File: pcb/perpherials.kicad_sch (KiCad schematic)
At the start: 9 parts, among them J4 TC2030, J6 050700622, J6 SBH11-PBPC-D05-ST-BK, U6 M24C64-FCS6TP/K, U7 BNO055

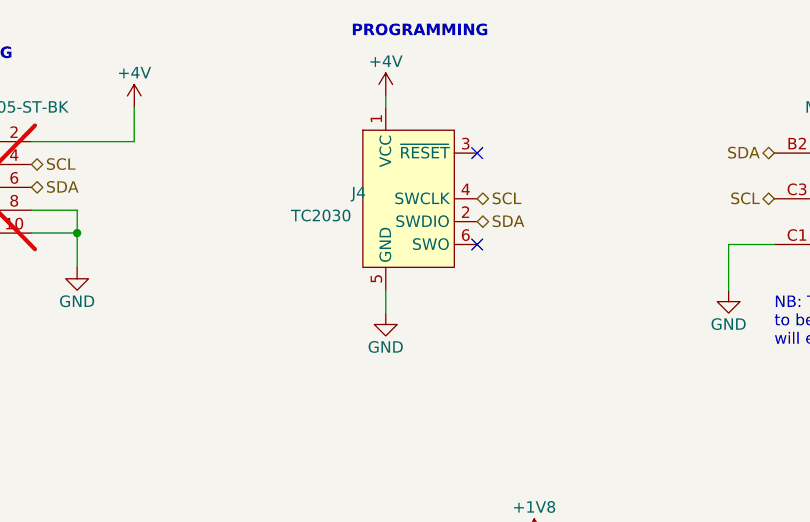
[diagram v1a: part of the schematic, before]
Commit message: Revision B
- Fix incorrect STG3856 symbol and make corresponding changes to PCB
- Flip bits 1 and 2 in probe interaces (fixes #1)
- Improve silkscreen
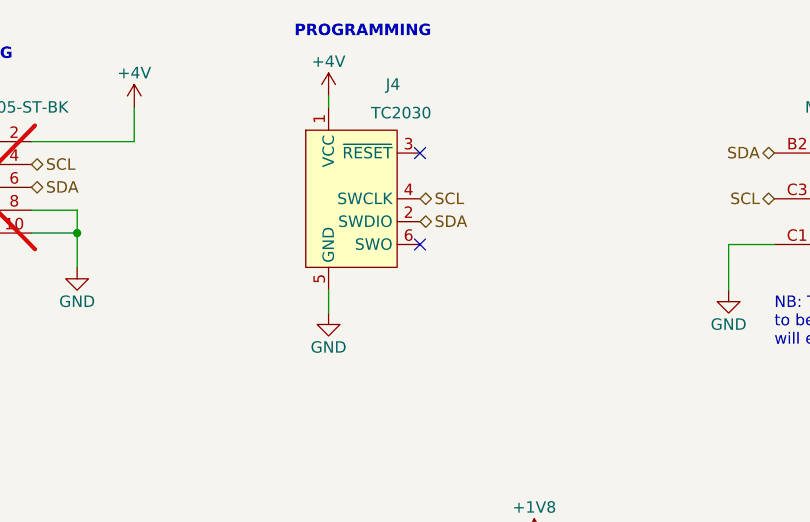
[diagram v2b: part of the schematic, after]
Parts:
- C25, C26, C27, C28, J4, J6, U6, U7: OEPS PN (none) -> ??
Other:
- moved on the sheet: J4
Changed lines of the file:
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@@
   (title_block
     (title "ONIX Neuropixels 2.0 Economical Headstage")
-    (rev "A")
+    (rev "B")
     (company "Open Ephys, Inc")
     (comment 1 "Jonathan P. Newman")
@@
   )
   (no_connect (at 114.3 127))
-  (no_connect (at 153.67 64.77))
+  (no_connect (at 147.32 64.77))
   (no_connect (at 144.78 127))
   (no_connect (at 114.3 119.38))
   (no_connect (at 144.78 114.3))
-  (no_connect (at 153.67 54.61))
+  (no_connect (at 147.32 54.61))
   (wire (pts (xy 115.57 53.34) (xy 115.57 49.53))
     (stroke (width 0) (type default))
@@
     (stroke (width 0) (type default))
   )
-  (wire (pts (xy 143.51 48.26) (xy 143.51 49.53))
-    (stroke (width 0) (type default))
-  )
-  (wire (pts (xy 143.51 69.85) (xy 143.51 72.39))
+  (wire (pts (xy 137.16 48.26) (xy 137.16 49.53))
+    (stroke (width 0) (type default))
+  )
+  (wire (pts (xy 137.16 69.85) (xy 137.16 72.39))
     (stroke (width 0) (type default))
   )
@@
     (effects (font (size 1.27 1.27) (thickness 0.254) bold) (justify left bottom))
   )
-  (text "PROGRAMMING" (at 139.7 41.91 0)
+  (text "PROGRAMMING" (at 133.35 41.91 0)
     (effects (font (size 1.27 1.27) (thickness 0.254) bold) (justify left bottom))
   )
@@
     (effects (font (size 1.27 1.27)) (justify right))
   )
-  (hierarchical_label "SDA" (shape bidirectional) (at 153.67 62.23 0) (fields_autoplaced)
+  (hierarchical_label "SDA" (shape bidirectional) (at 147.32 62.23 0) (fields_autoplaced)
     (effects (font (size 1.27 1.27)) (justify left))
   )
@@
     (effects (font (size 1.27 1.27)) (justify left))
   )
-  (hierarchical_label "SCL" (shape bidirectional) (at 153.67 59.69 0) (fields_autoplaced)
+  (hierarchical_label "SCL" (shape bidirectional) (at 147.32 59.69 0) (fields_autoplaced)
     (effects (font (size 1.27 1.27)) (justify left))
   )
-  (symbol (lib_id "power:GND") (at 143.51 72.39 0) (mirror y) (unit 1)
-    (in_bom yes) (on_board yes) (dnp no)
-    (property "Reference" "#PWR060" (at 143.51 78.74 0)
-      (effects (font (size 1.27 1.27)) hide)
-    )
-    (property "Value" "GND" (at 143.51 76.2 0)
-      (effects (font (size 1.27 1.27)))
-    )
-    (property "Footprint" "" (at 143.51 72.39 0)
-      (effects (font (size 1.27 1.27)) hide)
-    )
-    (property "Datasheet" "" (at 143.51 72.39 0)
+  (symbol (lib_id "power:GND") (at 137.16 72.39 0) (mirror y) (unit 1)
+    (in_bom yes) (on_board yes) (dnp no)
+    (property "Reference" "#PWR060" (at 137.16 78.74 0)
+      (effects (font (size 1.27 1.27)) hide)
+    )
+    (property "Value" "GND" (at 137.16 76.2 0)
+      (effects (font (size 1.27 1.27)))
+    )
+    (property "Footprint" "" (at 137.16 72.39 0)
+      (effects (font (size 1.27 1.27)) hide)
+    )
+    (property "Datasheet" "" (at 137.16 72.39 0)
       (effects (font (size 1.27 1.27)) hide)
     )
@@
     )
     (property "Tolerance" "" (at 129.54 127 0)
+      (effects (font (size 1.27 1.27)) hide)
+    )
+    (property "OEPS PN" "??" (at 129.54 127 0)
       (effects (font (size 1.27 1.27)) hide)
     )
@@
       (effects (font (size 1.27 1.27)) hide)
     )
+    (property "OEPS PN" "??" (at 214.63 125.73 0)
+      (effects (font (size 1.27 1.27)) hide)
+    )
     (pin "1")
     (pin "2")
@@
       (effects (font (size 1.27 1.27)) hide)
     )
+    (property "OEPS PN" "??" (at 217.17 59.69 0)
+      (effects (font (size 1.27 1.27)) hide)
+    )
     (pin "1")
     (pin "2")
@@
     )
     (property "Tolerance" "" (at 198.12 59.69 0)
+      (effects (font (size 1.27 1.27)) hide)
+    )
+    (property "OEPS PN" "??" (at 198.12 59.69 0)
       (effects (font (size 1.27 1.27)) hide)
     )
@@
       (effects (font (size 1.27 1.27)) hide)
     )
+    (property "OEPS PN" "??" (at 87.63 110.49 0)
+      (effects (font (size 1.27 1.27)) hide)
+    )
     (pin "1")
     (pin "2")
@@
     )
   )
-  (symbol (lib_id "Connector:Conn_ARM_SWD_TagConnect_TC2030") (at 146.05 59.69 0) (unit 1)
+  (symbol (lib_id "Connector:Conn_ARM_SWD_TagConnect_TC2030") (at 139.7 59.69 0) (unit 1)
     (in_bom no) (on_board yes) (dnp no)
-    (property "Reference" "J4" (at 139.7 59.055 0)
+    (property "Reference" "J4" (at 143.51 46.99 0)
       (effects (font (size 1.27 1.27)) (justify left))
     )
-    (property "Value" "TC2030" (at 139.7 61.595 0)
+    (property "Value" "TC2030" (at 148.59 50.165 0)
       (effects (font (size 1.27 1.27)) (justify right))
     )
-    (property "Footprint" "Connector:Tag-Connect_TC2030-IDC-FP_2x03_P1.27mm_Vertical" (at 146.05 77.47 0)
-      (effects (font (size 1.27 1.27)) hide)
-    )
-    (property "Datasheet" "https://www.tag-connect.com/wp-content/uploads/bsk-pdf-manager/TC2030-CTX_1.pdf" (at 146.05 74.93 0)
-      (effects (font (size 1.27 1.27)) hide)
-    )
-    (property "Tolerance" "" (at 146.05 59.69 0)
+    (property "Footprint" "Connector:Tag-Connect_TC2030-IDC-FP_2x03_P1.27mm_Vertical" (at 139.7 77.47 0)
+      (effects (font (size 1.27 1.27)) hide)
+    )
+    (property "Datasheet" "https://www.tag-connect.com/wp-content/uploads/bsk-pdf-manager/TC2030-CTX_1.pdf" (at 139.7 74.93 0)
+      (effects (font (size 1.27 1.27)) hide)
+    )
+    (property "Tolerance" "" (at 139.7 59.69 0)
+      (effects (font (size 1.27 1.27)) hide)
+    )
+    (property "OEPS PN" "??" (at 139.7 59.69 0)
       (effects (font (size 1.27 1.27)) hide)
     )
@@
     )
   )
-  (symbol (lib_id "power:+4V") (at 143.51 48.26 0) (mirror y) (unit 1)
+  (symbol (lib_id "power:+4V") (at 137.16 48.26 0) (mirror y) (unit 1)
     (in_bom yes) (on_board yes) (dnp no) (fields_autoplaced)
-    (property "Reference" "#PWR06" (at 143.51 52.07 0)
-      (effects (font (size 1.27 1.27)) hide)
-    )
-    (property "Value" "+4V" (at 143.51 44.45 0)
-      (effects (font (size 1.27 1.27)))
-    )
-    (property "Footprint" "" (at 143.51 48.26 0)
-      (effects (font (size 1.27 1.27)) hide)
-    )
-    (property "Datasheet" "" (at 143.51 48.26 0)
+    (property "Reference" "#PWR06" (at 137.16 52.07 0)
+      (effects (font (size 1.27 1.27)) hide)
+    )
+    (property "Value" "+4V" (at 137.16 44.45 0)
+      (effects (font (size 1.27 1.27)))
+    )
+    (property "Footprint" "" (at 137.16 48.26 0)
+      (effects (font (size 1.27 1.27)) hide)
+    )
+    (property "Datasheet" "" (at 137.16 48.26 0)
       (effects (font (size 1.27 1.27)) hide)
     )
@@
     )
     (property "Tolerance" "" (at 160.02 110.49 0)
+      (effects (font (size 1.27 1.27)) hide)
+    )
+    (property "OEPS PN" "??" (at 160.02 110.49 0)
       (effects (font (size 1.27 1.27)) hide)
     )
@@
       (effects (font (size 1.27 1.27)) hide)
     )
+    (property "OEPS PN" "??" (at 149.86 144.78 0)
+      (effects (font (size 1.27 1.27)) hide)
+    )
     (pin "1")
     (pin "2")
@@
       (effects (font (size 1.27 1.27)) hide)
     )
+    (property "OEPS PN" "??" (at 96.52 58.42 0)
+      (effects (font (size 1.27 1.27)) hide)
+    )
